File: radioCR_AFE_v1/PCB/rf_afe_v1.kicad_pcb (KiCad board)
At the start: 2 copper layers, 125.3 x 36.9 mm, 41 parts, among them J1 Conn_Coaxial, J2 Conn_Coaxial, U1 PHA-13LN, U3 PHA-13LN

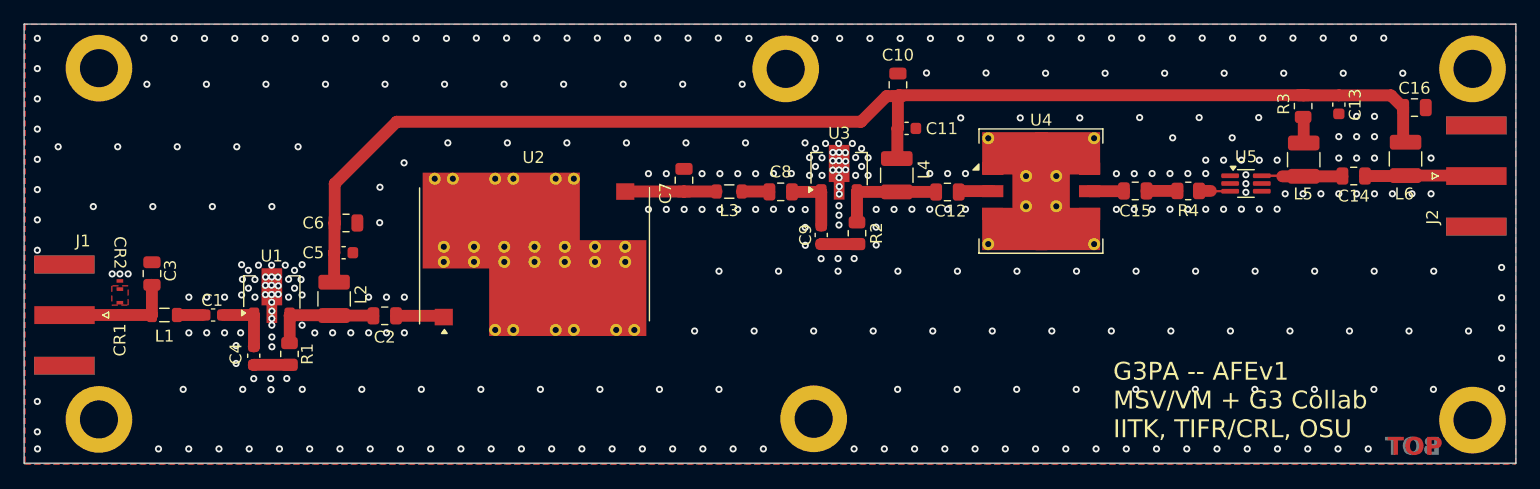
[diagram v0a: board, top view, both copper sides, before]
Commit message: Redone according to new line-up as per matlab sims. Mask removed from board edge too!
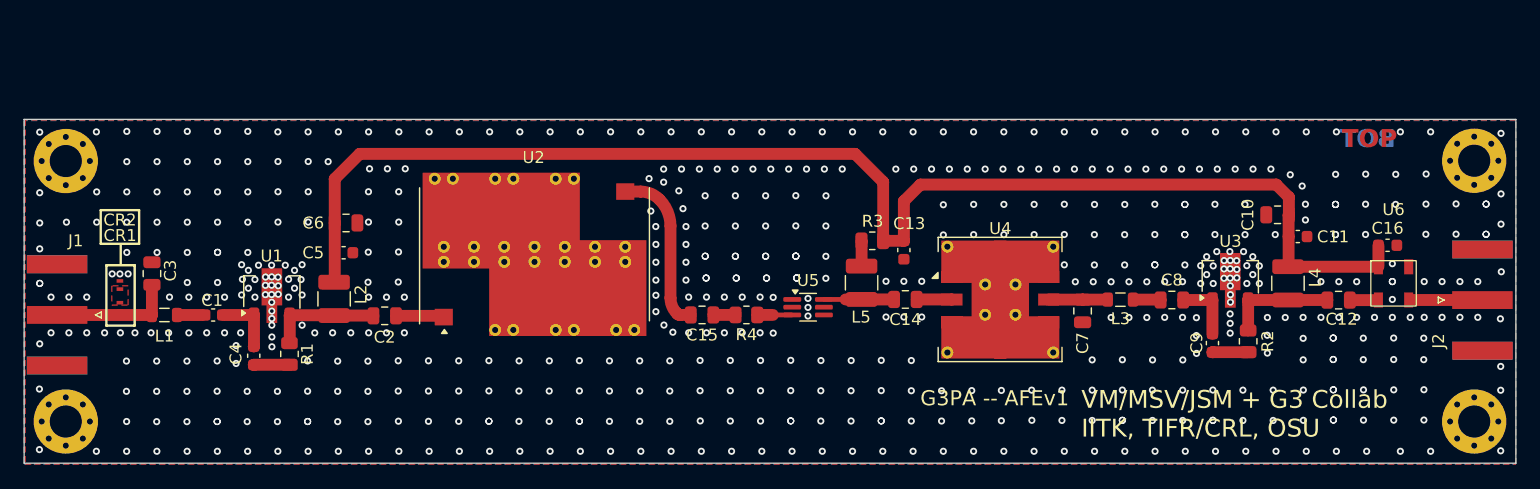
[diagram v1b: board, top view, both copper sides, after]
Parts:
- removed H3, H4: MountingHole_Pad, MountingHole:MountingHole_3.2mm_M3_DIN965_Pad
- removed L6: L_Small, Inductor_SMD:L_1210_3225Metric
- added U6: TCBT-6G+, minickts_kicad:GU1604, F.Cu at (201.7, 97.1)
- C16: footprint Capacitor_SMD:C_0805_2012Metric -> Capacitor_SMD:C_0603_1608Metric
- H1, H2, H5, H6: footprint MountingHole:MountingHole_3.2mm_M3_DIN965_Pad -> MountingHole:MountingHole_2.7mm_M2.5_Pad_Via
- U2: value ~ -> BSF108+
- U4: value ~ -> RBP188
- U5: value ~ -> PSA8A+
- moved C14 39.1 mm to (160.7, 98.4)
- moved L5 38.5 mm to (157.1, 97.0)
- moved R4 38.5 mm to (147.4, 99.7)
- moved C13 38.5 mm to (160.6, 94.3)
- moved U5 38.2 mm to (152.6, 99.1)
- moved R3 37.9 mm to (157.9, 93.5), turned to 0 degrees
- moved C15 37.8 mm to (143.7, 99.7)
- moved C7 35.2 mm to (175.6, 99.4), turned to 90 degrees
- moved C12 34.1 mm to (197.1, 98.5)
- moved C8 34.1 mm to (183.1, 98.5)
- moved L4 34.1 mm to (192.9, 97.1)
- moved C11 34.1 mm to (193.7, 93.1)
- moved C9 34.1 mm to (186.5, 102.1)
- moved L3 34.1 mm to (178.8, 98.4)
- moved R2 34.1 mm to (189.5, 101.9)
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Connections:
- C12 pad 2: Net-(U4-RF_IN) -> Net-(U6-RF)
- C14 pad 1: Net-(J2-In) -> Net-(U4-RF_IN)
- C15 pad 2: Net-(U4-RF_OUT) -> Net-(U2-RFOUT)
- C16 pad 1: GND -> +5V
- C16 pad 2: +5V -> GND
- C7 pad 2: Net-(U2-RFOUT) -> Net-(U4-RF_OUT)
- L3 pad 1: Net-(U2-RFOUT) -> Net-(U4-RF_OUT)
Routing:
- net Net-(U2-RFOUT): track 7.68 -> 14.2 mm
- net +5V: track 109.9 -> 115.1 mm
- net Net-(J2-In): track 9.24 -> 5.41 mm
- net Net-(U6-RF): track 0.00 -> 2.19 mm
- net Net-(U4-RF_OUT): track 2.89 -> 4.89 mm
- net Net-(U5-RF-OUT/Vdd): track 6.80 -> 5.89 mm
- net Net-(C15-Pad1): track 2.59 -> 1.86 mm
- net GND: vias 354 -> 582
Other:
- board size 125.3 x 36.9 mm -> 125.3 x 28.9 mm
- board text added: "G3PA -- AFEv1"
- board text added: "VM/MSV/JSM + G3 Collab IITK, TIFR/CRL, OSU"
- board text removed: "G3PA -- AFEv1 MSV/VM + G3 Collab IITK, TIFR/CRL, OSU"
